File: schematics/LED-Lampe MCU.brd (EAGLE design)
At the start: 100 x 36.3 mm, 81 parts, among them IC1 4052D, IC2 TSOP34836, IC3 TSOP34836, IC4 AT45DB161D-SU, IC5 MCP604ST, Q1 CSTCR6M00G53Z, Q2 BSS138, Q3 BSS138

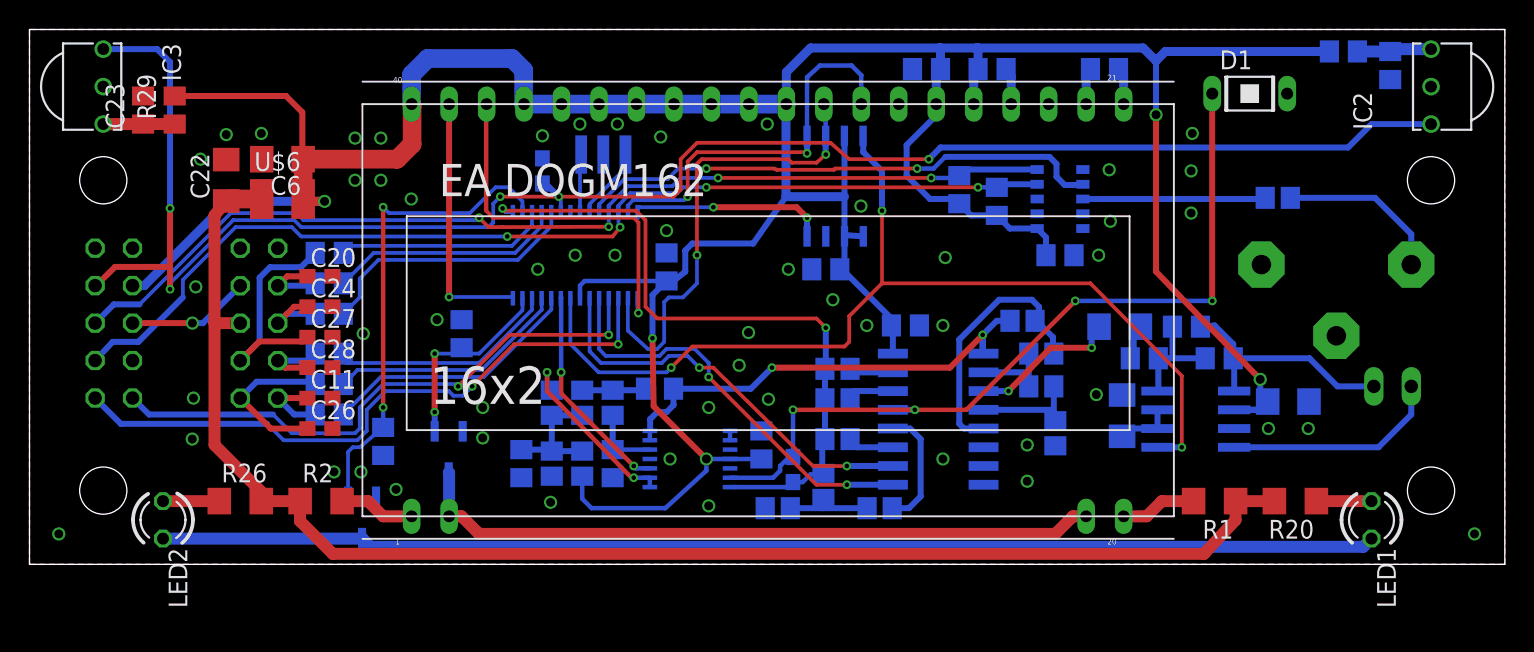
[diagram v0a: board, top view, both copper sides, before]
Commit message: - improved placement of IR-LED, IR-Receiver, Photodiode - removed unused devices
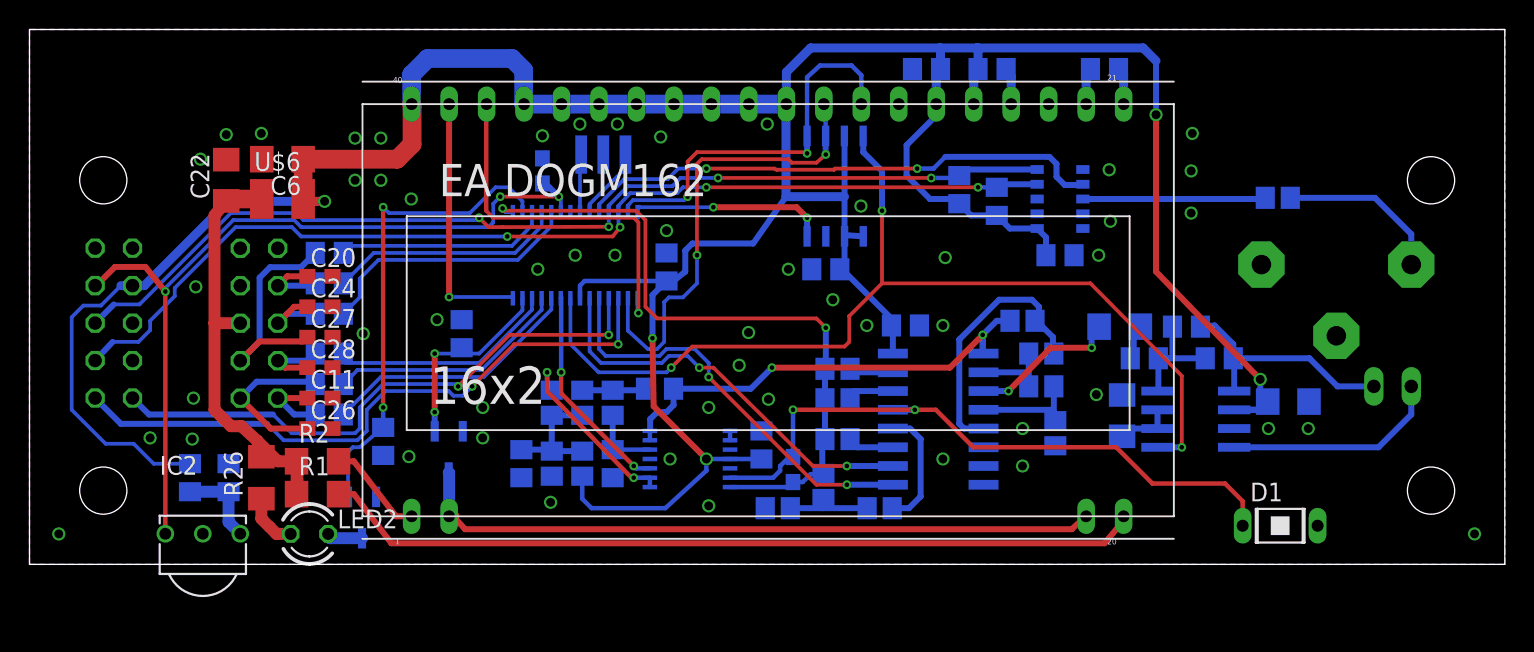
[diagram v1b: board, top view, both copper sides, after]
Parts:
- removed C23: 1µF, rcl:C0805
- removed IC3: TSOP34836, vishay-1:TSOP348
- removed LED1: SFH409, led:LED3MM
- removed R20: 4,7, rcl:R1206
- removed R29: 470, rcl:R0805
- moved IC2 88.6 mm to (11.7, 2.08), turned to 0 degrees
- moved C12 83.6 mm to (13.5, 5.87), turned to 90 degrees
- moved R12 83.4 mm to (10.9, 5.87), turned to 90 degrees
- moved R1 60.8 mm to (19.5, 4.76), turned to 0 degrees
- moved D1 29.4 mm to (84.8, 2.62)
- moved LED2 9.97 mm to (19.0, 2.06), turned to 0 degrees
- moved R2 2.71 mm to (19.5, 6.99)
- moved R26 2.14 mm to (15.7, 5.87), turned to 90 degrees
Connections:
- removed net N$43: JP1.5, JP2.4
- removed net N$48: LED1.A, R20.1
- removed net N$54: C23.1, IC3.3, R29.1
- net +3V3: no longer R29.2
- net GND: no longer C23.2, IC3.2
- net N$46: no longer LED1.K
- net P1.5: no longer IC3.1
- net V+: no longer R20.2
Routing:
- net N$46: track 82.4 -> 2.49 mm
- net V+: track 99.6 -> 30.8 mm
- net P1.5: track 122.2 -> 55.9 mm, vias 5 -> 3
- net N$7: track 5.17 -> 55.9 mm
- net N$33: track 55.2 -> 44.4 mm, vias 4 -> 2
- net N$43: track 8.35 -> 0.00 mm, vias 1 -> 0
- net N$54: track 4.85 -> 0.00 mm
- net N$48: track 3.74 -> 0.00 mm
- net +3V3: track 250.0 -> 246.5 mm
- net N$8: track 5.14 -> 6.79 mm
- net N$6: track 5.09 -> 5.80 mm

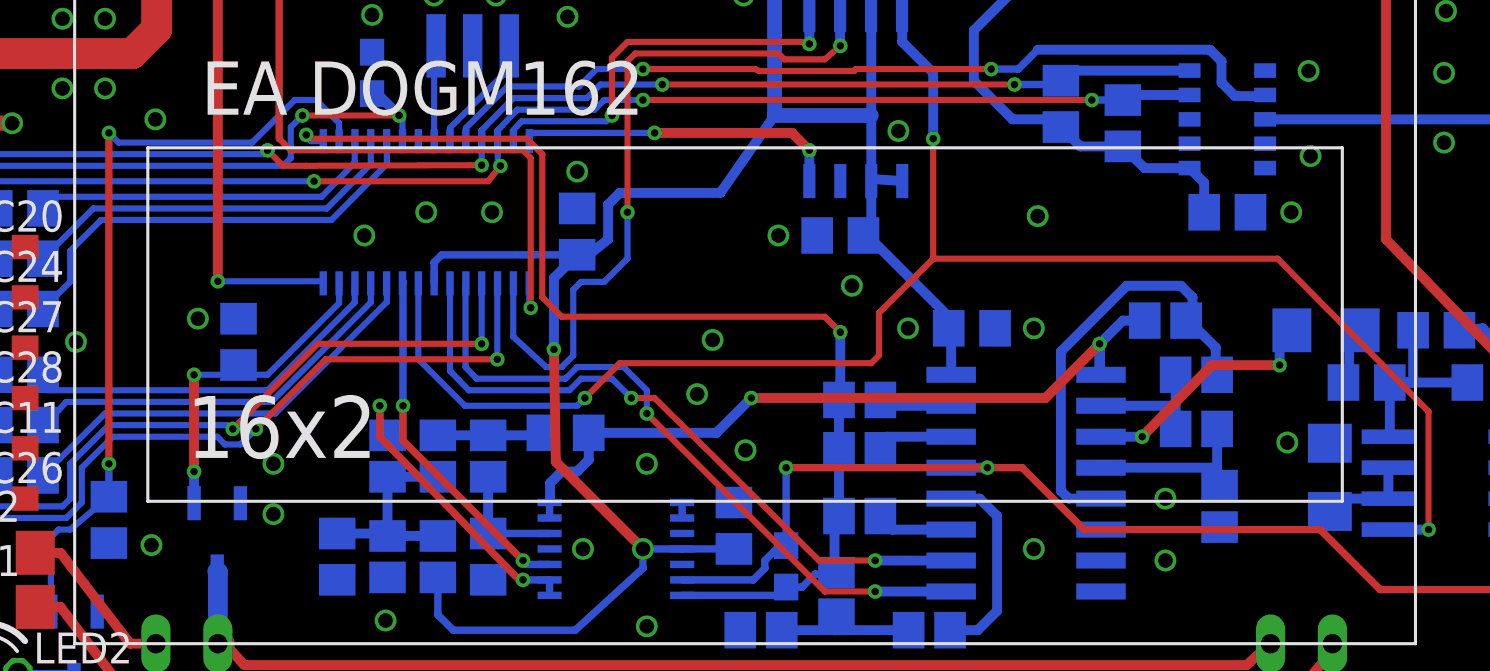
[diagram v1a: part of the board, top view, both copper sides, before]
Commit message: 
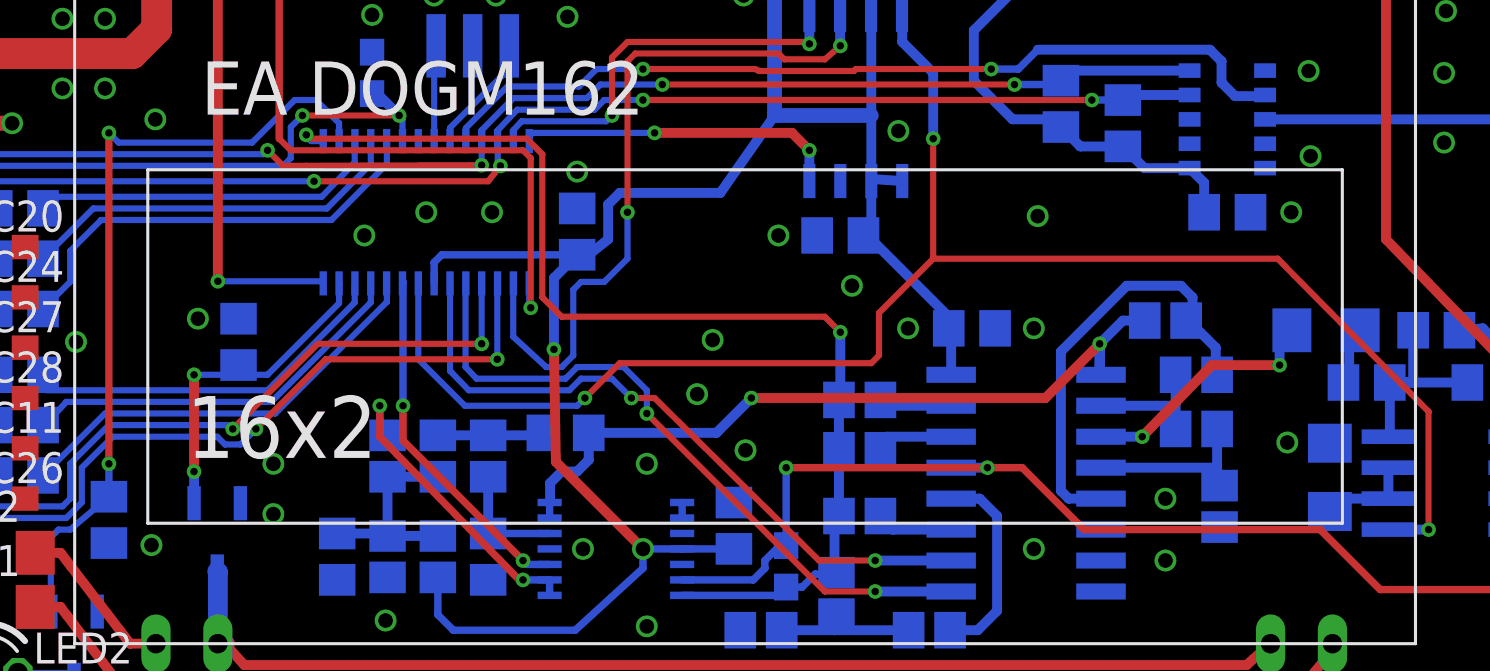
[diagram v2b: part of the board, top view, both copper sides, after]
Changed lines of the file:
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@@
 <layer number="27" name="tValues" color="7" fill="1" visible="no" active="yes"/>
 <layer number="28" name="bValues" color="7" fill="1" visible="no" active="yes"/>
-<layer number="29" name="tStop" color="7" fill="3" visible="no" active="yes"/>
-<layer number="30" name="bStop" color="7" fill="6" visible="no" active="yes"/>
-<layer number="31" name="tCream" color="7" fill="4" visible="no" active="yes"/>
-<layer number="32" name="bCream" color="7" fill="5" visible="no" active="yes"/>
-<layer number="33" name="tFinish" color="6" fill="3" visible="no" active="yes"/>
-<layer number="34" name="bFinish" color="6" fill="6" visible="no" active="yes"/>
-<layer number="35" name="tGlue" color="7" fill="4" visible="no" active="yes"/>
-<layer number="36" name="bGlue" color="7" fill="5" visible="no" active="yes"/>
-<layer number="37" name="tTest" color="7" fill="1" visible="no" active="yes"/>
-<layer number="38" name="bTest" color="7" fill="1" visible="no" active="yes"/>
+<layer number="29" name="tStop" color="7" fill="3" visible="yes" active="yes"/>
+<layer number="30" name="bStop" color="7" fill="6" visible="yes" active="yes"/>
+<layer number="31" name="tCream" color="7" fill="4" visible="yes" active="yes"/>
+<layer number="32" name="bCream" color="7" fill="5" visible="yes" active="yes"/>
+<layer number="33" name="tFinish" color="6" fill="3" visible="yes" active="yes"/>
+<layer number="34" name="bFinish" color="6" fill="6" visible="yes" active="yes"/>
+<layer number="35" name="tGlue" color="7" fill="4" visible="yes" active="yes"/>
+<layer number="36" name="bGlue" color="7" fill="5" visible="yes" active="yes"/>
+<layer number="37" name="tTest" color="7" fill="1" visible="yes" active="yes"/>
+<layer number="38" name="bTest" color="7" fill="1" visible="yes" active="yes"/>
 <layer number="39" name="tKeepout" color="4" fill="11" visible="yes" active="yes"/>
-<layer number="40" name="bKeepout" color="1" fill="11" visible="no" active="yes"/>
+<layer number="40" name="bKeepout" color="1" fill="11" visible="yes" active="yes"/>
 <layer number="41" name="tRestrict" color="4" fill="10" visible="yes" active="yes"/>
-<layer number="42" name="bRestrict" color="1" fill="10" visible="no" active="yes"/>
+<layer number="42" name="bRestrict" color="1" fill="10" visible="yes" active="yes"/>
 <layer number="43" name="vRestrict" color="2" fill="10" visible="yes" active="yes"/>
 <layer number="44" name="Drills" color="7" fill="1" visible="yes" active="yes"/>
